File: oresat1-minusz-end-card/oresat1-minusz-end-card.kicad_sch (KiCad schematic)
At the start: 36 parts, among them J1 J-SAMTEC-TFM-120-01-L-D-RA, J2 U.FL-R-SMT-1, J3 Harwin M55-7101242R, J5 Harwin M55-7101242R

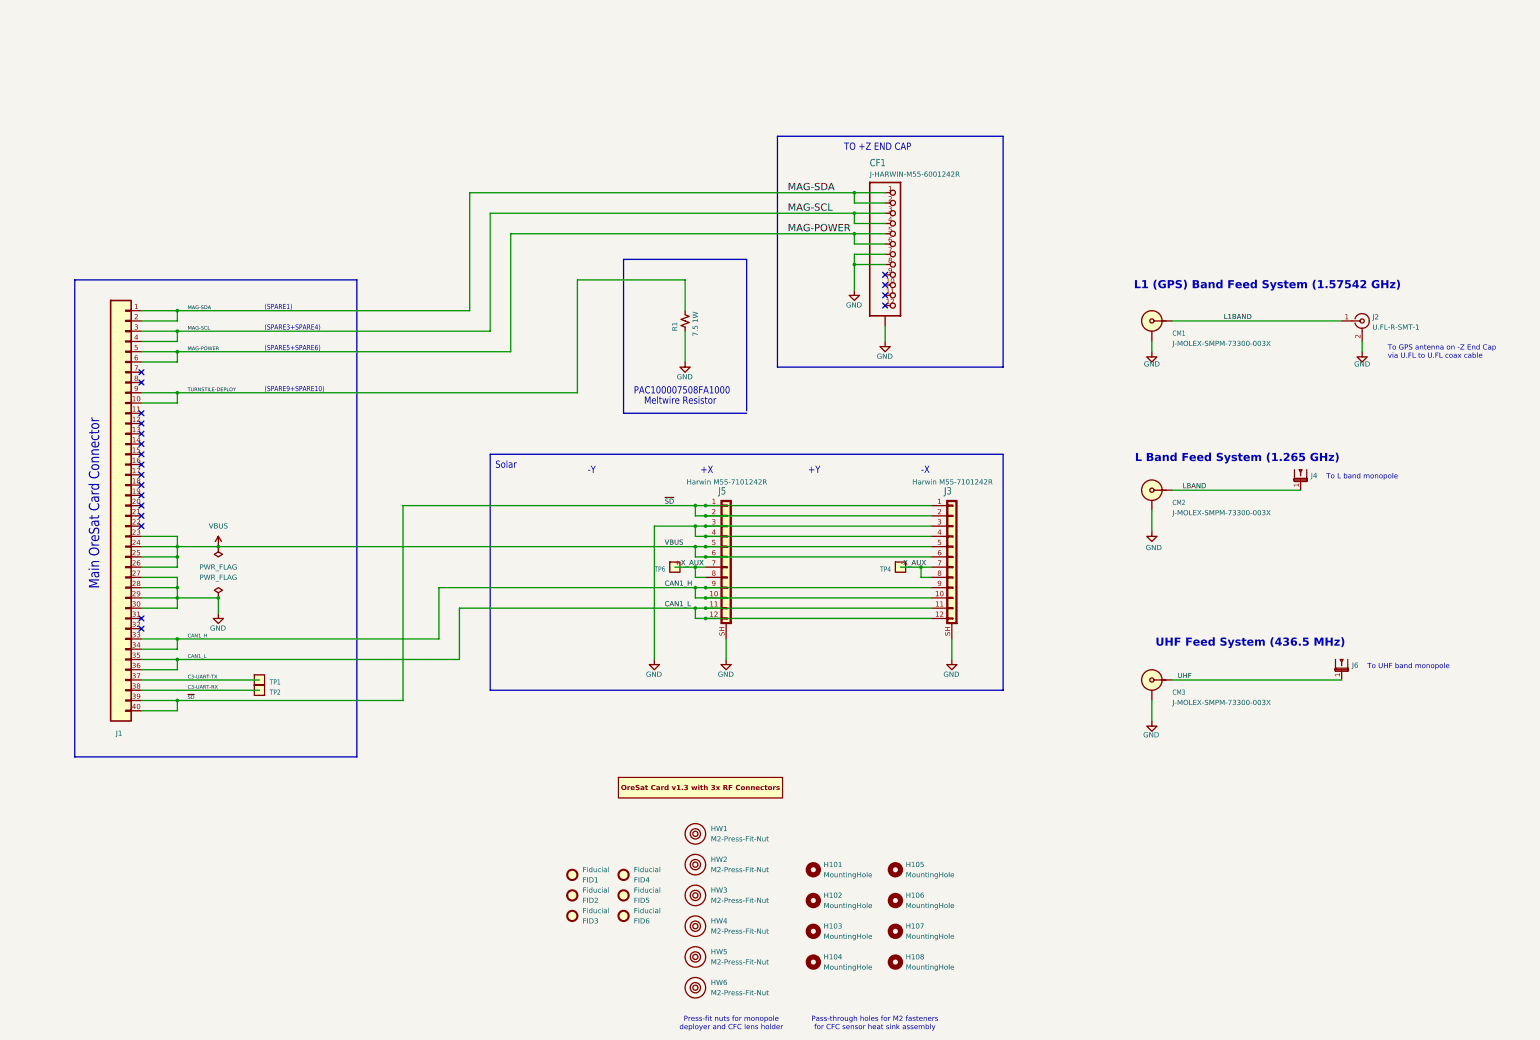
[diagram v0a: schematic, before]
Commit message: add OPD and deployer circuitry
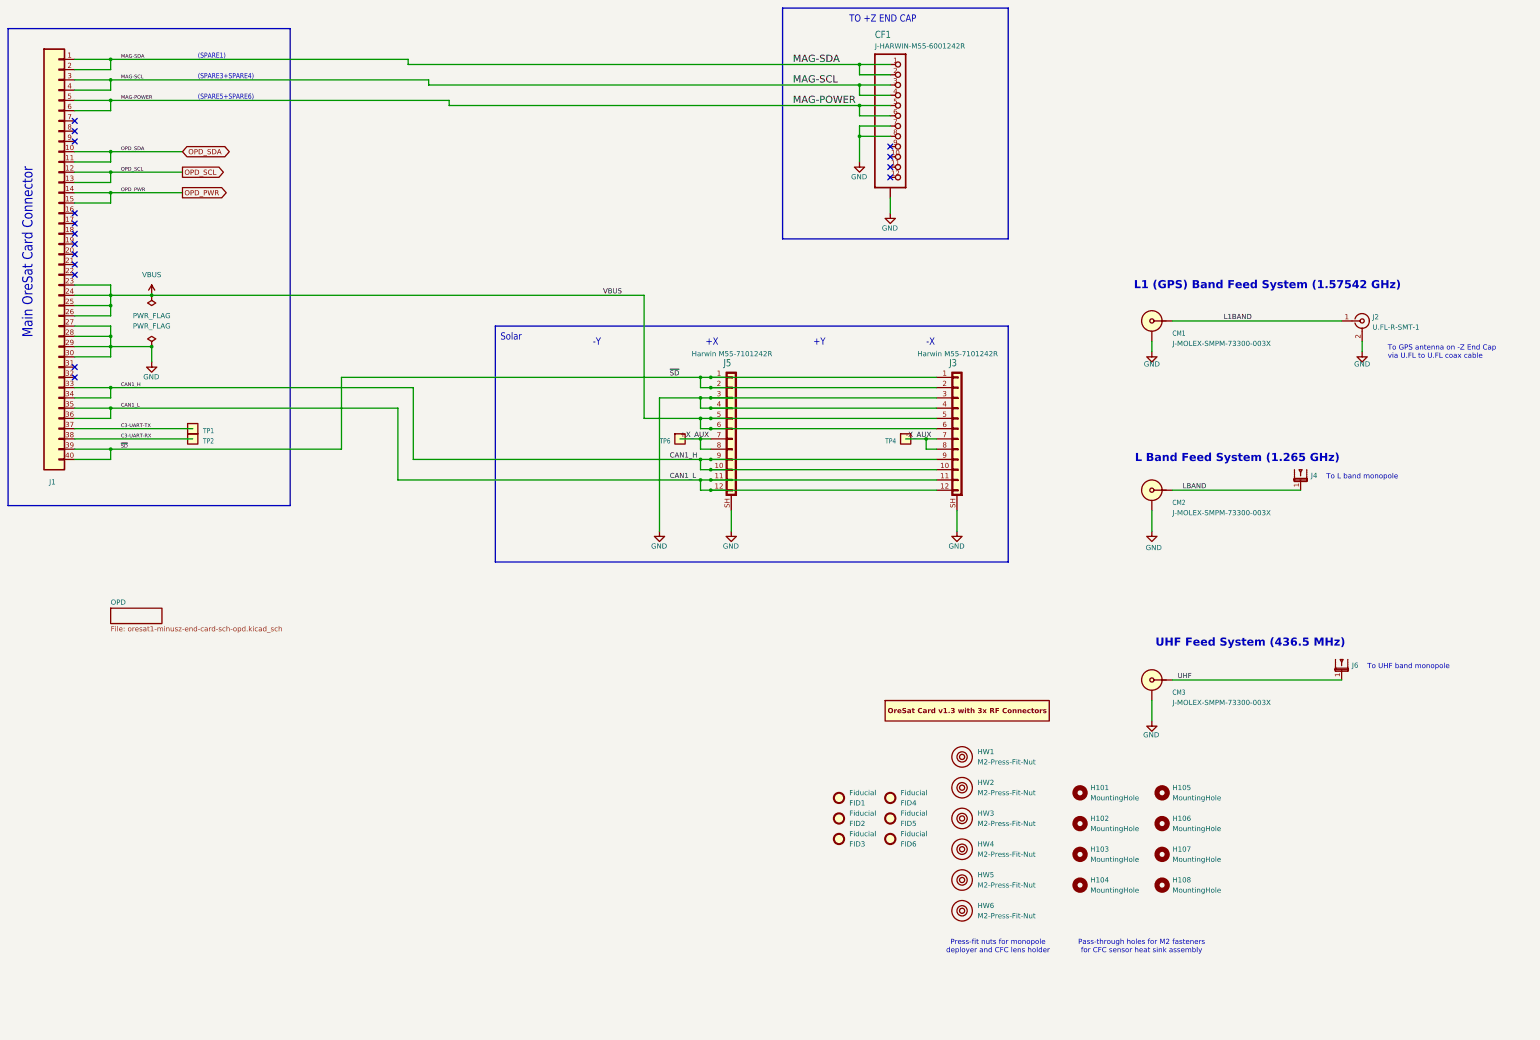
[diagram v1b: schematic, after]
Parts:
- removed R1: 7.5 1W, oresat-passives:R-PAC100-FOR-MELTWIRE, symbol Device:R_Small_US
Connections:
- net OPD_SDA: now reaches J1.11
- net OPD_SDA: now also J1.10
- net OPD_SCL: now reaches J1.12
- net OPD_SCL: now also J1.13
- net OPD_PWR: now reaches J1.14
- net OPD_PWR: now also J1.15
- net TURNSTILE-DEPLOY: no longer names the net of J1.9
- net TURNSTILE-DEPLOY: no longer J1.10
- no-connect marks 20 -> 16
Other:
- added sheet OPD (oresat1-minusz-end-card-sch-opd.kicad_sch)
- note removed: "(SPARE9+SPARE10)"
- note removed: "Meltwire Resistor"
- note removed: "PAC100007508FA1000"
- moved on the sheet: CF1, FID1, FID2, FID3, FID4, FID5, FID6, H101, H102, H103, H104, H105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

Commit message: v1.1
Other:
- company: (none) -> Portland State Aerospace Society
- title: OreSat0.5 -Z End Card -> OreSat1 -Z End Card
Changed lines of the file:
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@@
 	(generator "eeschema")
 	(generator_version "9.0")
-	(paper "USLedger")
+	(paper "B")
 	(title_block
-		(title "OreSat0.5 -Z End Card")
-		(date "2024-03-31")
-		(rev "1.3")
+		(title "OreSat1 -Z End Card")
+		(date "2026-02-10")
+		(rev "v1.1")
+		(company "Portland State Aerospace Society")
 	)
 	(text "+X"
